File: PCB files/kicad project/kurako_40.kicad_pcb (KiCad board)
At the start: 2 copper layers, 226 x 76 mm, 121 parts, among them J1 conn, P1 USB_C_Plug_USB2.0, SW1 TAB, SW10 S, SW11 X, SW12 PROG, SW13 E, SW14 D, SW15 C, SW16 ALT, SW17 R, SW18 F, SW19 V, SW2 ESC, SW20 SPACE, SW21 T, SW22 G, SW23 B, SW24 Y, SW25 H, SW26 N, SW27 LOWER, SW28 U, SW29 J, SW3 SHIFT, SW30 M, SW31 RAISE, SW32 I, SW33 K, SW34 ,, SW35 /, SW36 O, SW37 L, SW38 ., SW39 LEFT, SW4 CTRL, SW40 P, SW41 ;, SW42 UP, SW43 DOWN, SW44 BKSP, SW45 ', SW46 ENTER, SW47 RIGHT, SW48 SW_SPST, SW5 Q, SW6 A, SW7 Z, SW8 WIN, SW9 W, U1 ATmega32U4-AU, Y1 16 Mhz

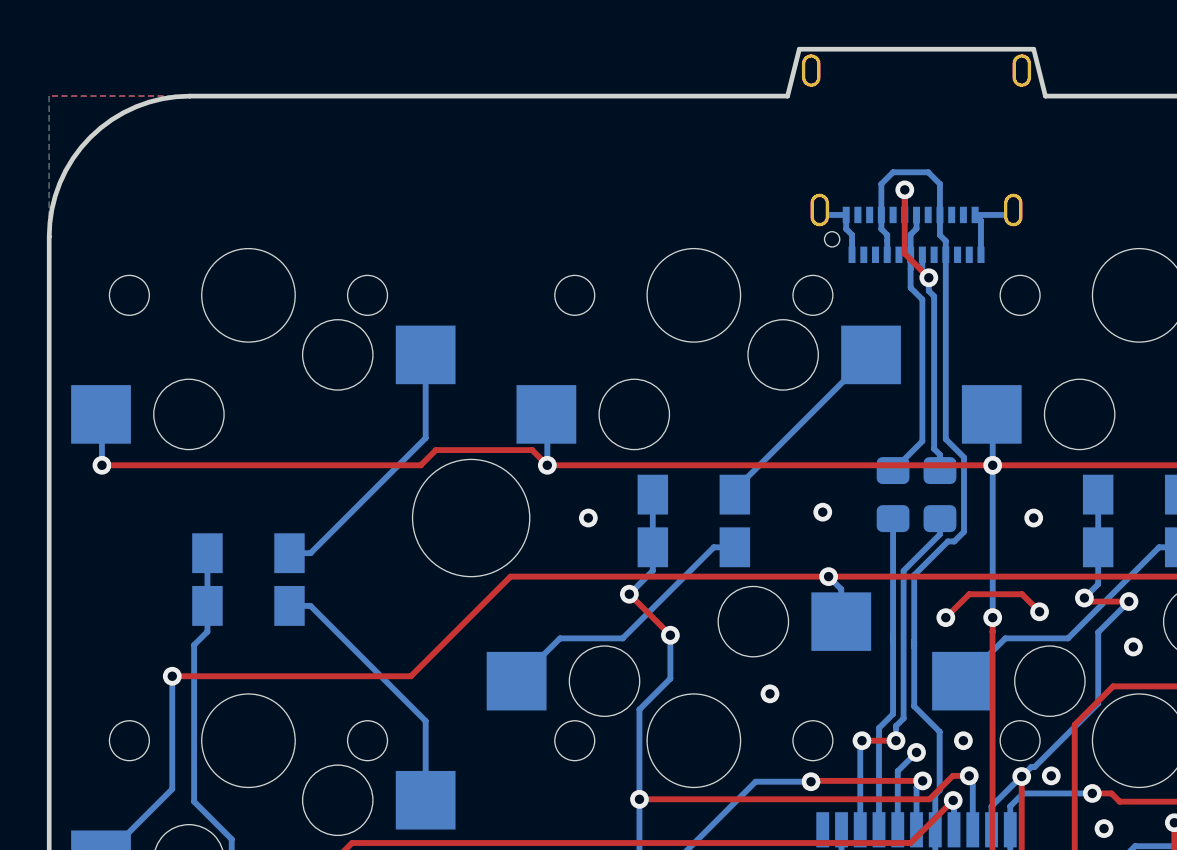
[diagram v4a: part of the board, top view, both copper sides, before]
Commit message: usb c updates
chose better USB connector for hand soldering
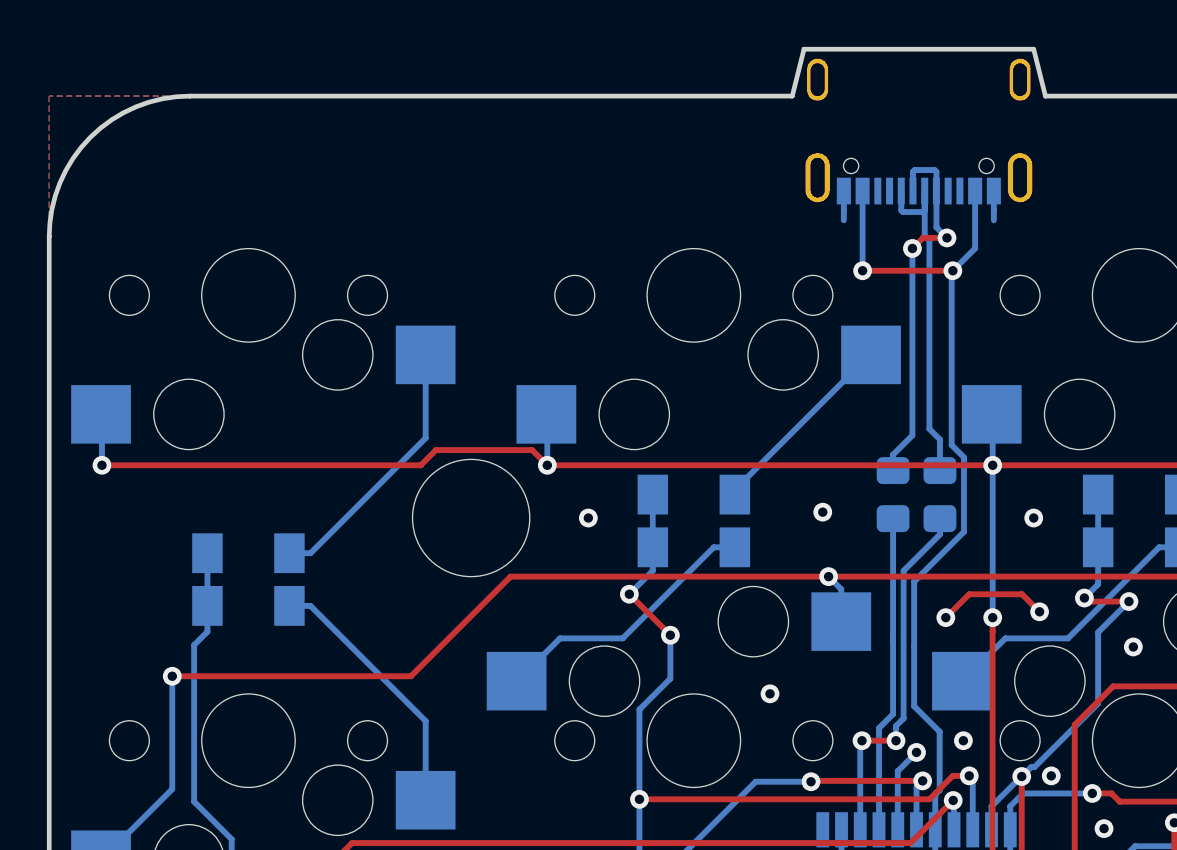
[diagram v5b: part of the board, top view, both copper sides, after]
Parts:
- P1: footprint Connector_USB:USB_C_Receptacle_Amphenol_12401610E4-2A -> 12402012E212A_USB-C:AMPHENOL_12402012E212A
- moved P1 2.45 mm to (78.6, 60.8)
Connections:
- net Net-(P1-PadA6) renamed D1+
- net Net-(P1-PadA7) renamed D1-
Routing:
- net D1+: track 11.7 -> 16.4 mm, vias 0 -> 2
- net GND: track 26.8 -> 22.7 mm
- net VBUS: track 99.0 -> 99.7 mm, vias 4 -> 6
- net D1-: track 14.8 -> 14.9 mm, vias 2 -> 0
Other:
- outline, holes or cut-outs redrawn
- board text added: "kurako_40 Rev 1.4 Nathan Steward"
- board text removed: "kurako_40 Rev 1.3 Nathan Steward"
